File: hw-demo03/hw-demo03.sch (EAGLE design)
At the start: 40 parts, among them IC3 MCP2562T, IC4 STM32F042, Q1 BTS500101TADATMA2, Q2 BTS500101TADATMA2, SW1+ VP0265840000G, SW2+ VP0265840000G

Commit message: first routing pass completed
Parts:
- removed J_IS1: 0R0, rcl:R-US_0207/12
- added J_5VCAN: 000, rcl:R-US_0207/15
- added R_ISPD2: 1K0, rcl:R-US_0204/7
- J_IS2: value 0R0 -> 000; device rcl:R-US_0207/12 -> rcl:R-US_0207/15
- R_GND2: value 0R0 -> 000
- R_IN1: device rcl:R-US_0207/12 -> rcl:R-US_0207/10
- R_IN2, R_IS1, R_IS2, R_ISPD1: device rcl:R-US_0207/12 -> rcl:R-US_0204/7
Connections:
- net +5V: now also J_5VCAN.2; no longer CCAN1.1, IC3.VDD
- net ADC3: now also IC4.PA0, J_IS2.2; no longer R_IS2.2
- net CTL1: no longer IC4.PA13
- net CTL2: now also IC4.PA15; no longer IC4.PB4
- net GND: now also R_ISPD2.1
- net IS: now also R_IS1.1; no longer J_IS1.1
- net N$2: now also J_IS2.1, R_IS2.2; no longer J_IS1.2, R_IS1.1
- net N$6: now also R_IS2.1, R_ISPD2.2; no longer J_IS2.1
- net N$7: now also CCAN1.1, IC3.VDD, J_5VCAN.1; no longer J_IS2.2, R_IS2.1
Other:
- moved on the sheet: J_IS2, R_IS1, R_IS2

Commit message: add cap on voltage divider, more stitching
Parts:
- added CDIV: 100n, rcl:C-USC0603K
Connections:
- net ADC2: now also CDIV.1
- net GND: now also CDIV.2, IC3.STBY
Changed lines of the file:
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@@
 <part name="R_IS2" library="rcl" deviceset="R-US_" device="0204/7" value="10K"/>
 <part name="J_5VCAN" library="rcl" deviceset="R-US_" device="0207/15" value="000"/>
+<part name="CDIV" library="rcl" deviceset="C-US" device="C0603K" value="100n"/>
 </parts>
 <sheets>
@@
 <instance part="R_IS2" gate="G$1" x="172.72" y="114.3" rot="R180"/>
 <instance part="J_5VCAN" gate="G$1" x="60.96" y="226.06" rot="R180"/>
+<instance part="CDIV" gate="G$1" x="83.82" y="121.92"/>
 </instances>
 <busses>
@@
 <pinref part="CCAN2" gate="G$1" pin="2"/>
 <wire x1="134.62" y1="198.12" x2="134.62" y2="195.58" width="0.1524" layer="91"/>
-<wire x1="134.62" y1="195.58" x2="76.2" y2="195.58" width="0.1524" layer="91"/>
+<wire x1="134.62" y1="195.58" x2="129.54" y2="195.58" width="0.1524" layer="91"/>
 <junction x="76.2" y="195.58"/>
 <pinref part="CAN" gate="-2" pin="KL"/>
+<wire x1="129.54" y1="195.58" x2="76.2" y2="195.58" width="0.1524" layer="91"/>
 <wire x1="157.48" y1="220.98" x2="152.4" y2="220.98" width="0.1524" layer="91"/>
 <wire x1="152.4" y1="220.98" x2="152.4" y2="195.58" width="0.1524" layer="91"/>
 <wire x1="152.4" y1="195.58" x2="134.62" y2="195.58" width="0.1524" layer="91"/>
 <junction x="134.62" y="195.58"/>
+<pinref part="IC3" gate="G$1" pin="STBY"/>
+<wire x1="124.46" y1="215.9" x2="129.54" y2="215.9" width="0.1524" layer="91"/>
+<wire x1="129.54" y1="215.9" x2="129.54" y2="195.58" width="0.1524" layer="91"/>
+<junction x="129.54" y="195.58"/>
 </segment>
 <segment>
@@
 <segment>
 <pinref part="RDIV2" gate="G$1" pin="1"/>
-<wire x1="76.2" y1="109.22" x2="76.2" y2="116.84" width="0.1524" layer="91"/>
+<wire x1="76.2" y1="109.22" x2="76.2" y2="114.3" width="0.1524" layer="91"/>
 <pinref part="GND9" gate="1" pin="GND"/>
+<pinref part="CDIV" gate="G$1" pin="2"/>
+<wire x1="76.2" y1="114.3" x2="76.2" y2="116.84" width="0.1524" layer="91"/>
+<wire x1="76.2" y1="114.3" x2="83.82" y2="114.3" width="0.1524" layer="91"/>
+<wire x1="83.82" y1="114.3" x2="83.82" y2="116.84" width="0.1524" layer="91"/>
+<junction x="76.2" y="114.3"/>
 </segment>
 <segment>
@@
 <wire x1="76.2" y1="127" x2="76.2" y2="129.54" width="0.1524" layer="91"/>
 <wire x1="76.2" y1="129.54" x2="76.2" y2="134.62" width="0.1524" layer="91"/>
-<wire x1="86.36" y1="129.54" x2="76.2" y2="129.54" width="0.1524" layer="91"/>
+<wire x1="91.44" y1="129.54" x2="83.82" y2="129.54" width="0.1524" layer="91"/>
 <junction x="76.2" y="129.54"/>
-<label x="86.36" y="129.54" size="1.27" layer="95" xref="yes"/>
-</segment>
-</net>
+<label x="91.44" y="129.54" size="1.27" layer="95" xref="yes"/>
+<pinref part="CDIV" gate="G$1" pin="1"/>
+<wire x1="83.82" y1="129.54" x2="76.2" y2="129.54" width="0.1524" layer="91"/>
+<wire x1="83.82" y1="124.46" x2="83.82" y2="129.54" width="0.1524" layer="91"/>
+<junction x="83.82" y="129.54"/>
+</segment>
+</net>

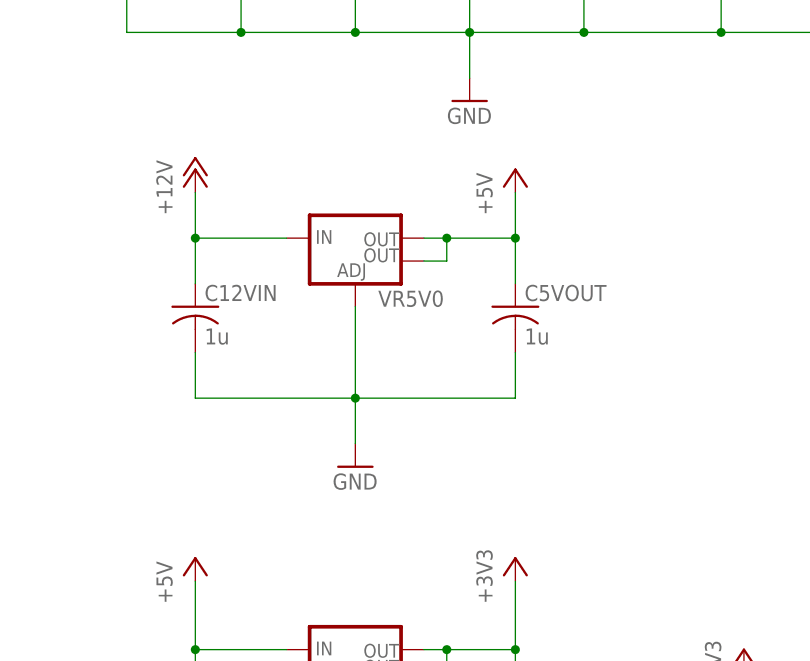
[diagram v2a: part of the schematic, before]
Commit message: added inexpensive 5v smps module to replace 5v linear
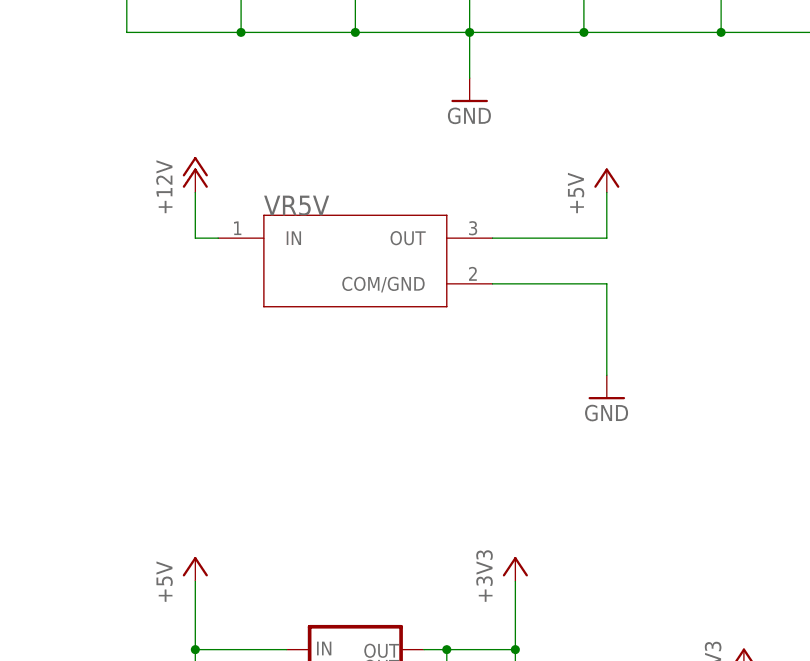
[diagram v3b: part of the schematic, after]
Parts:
- removed C12VIN: 1u, rcl:C-USC1206K
- removed C5VOUT: 1u, rcl:C-USC0805K
- removed VR5V0: (no value), SparkFun-PowerIC:V_REG_LM1117SOT223
- added VR5V: OKI-78SR-5/1.5-W36-C, OKI-78SR-5_1.5-W36-C:OKI-78SR-5/1.5-W36-C
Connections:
- net +12V: now also VR5V.IN; no longer C12VIN.1, VR5V0.IN
- net +5V: now also VR5V.OUT; no longer C5VOUT.1, VR5V0.OUT, VR5V0.OUT@1
- net GND: now also VR5V.COM/GND; no longer C12VIN.2, C5VOUT.2, VR5V0.ADJ
